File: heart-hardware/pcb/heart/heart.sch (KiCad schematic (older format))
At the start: 64 parts, among them J1 3V0, J2 DIO, J3 CLK, J4 GND, J5 TOUCH_KEY, SW1 SW_SPDT, U1 STM32L031F6Px, U2 TCA6416APWR, U3 LIS3DH, U4 Holtek-Semicon-BS812A-1

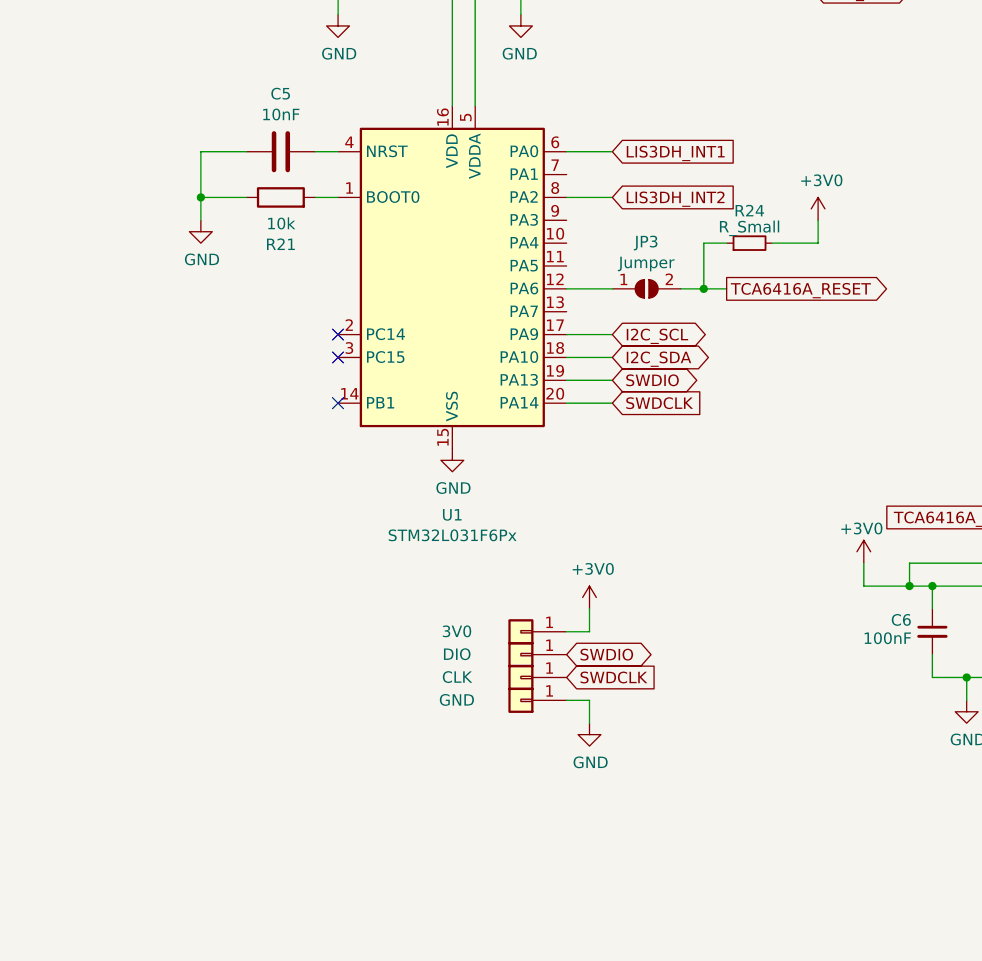
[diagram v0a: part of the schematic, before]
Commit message: Added jumper to choose interuppt lines
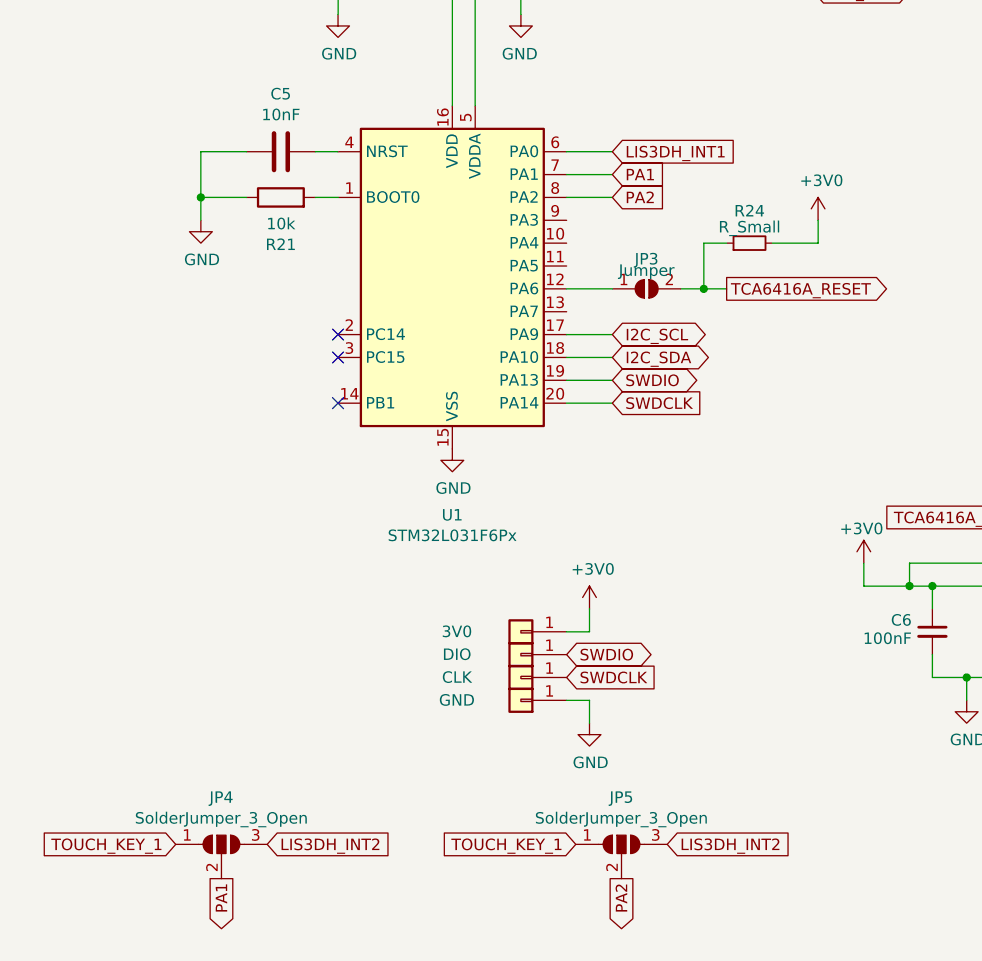
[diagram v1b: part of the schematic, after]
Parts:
- added JP4, JP5: SolderJumper_3_Open, Jumper:SolderJumper-3_P1.3mm_Open_RoundedPad1.0x1.5mm_NumberLabels, symbol Jumper:SolderJumper_3_Open
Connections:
- net LIS3DH_INT2: now also JP4.3 (B), JP5.3 (B); no longer U1.8 (PA2)
- net TOUCH_KEY_1: now also JP4.1 (A), JP5.1 (A)
- net PA1: now reaches U1.7 (PA1)
- net PA1: now also JP4.2 (C)
- new net PA2: JP5.2 (C), U1.8 (PA2)
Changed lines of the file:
@@
 	9100 4300 8700 4300
-Wire Wire Line
-	3100 4300 2900 4300
 Wire Wire Line
 	9500 3900 9500 3800
@@
 	1    0    0    -1
 $EndComp
-Text GLabel 3100 4300 2    50   Input ~ 0
+Text GLabel 1590 7130 2    50   Input ~ 0
 LIS3DH_INT2
 $Comp
@@
 U 1 1 61D85D1A
 P 3250 4700
-F 0 "JP3" H 3250 4905 50  0000 C CNN
-F 1 "Jumper" H 3250 4814 50  0000 C CNN
+F 0 "JP3" H 3250 4830 50  0000 C CNN
+F 1 "Jumper" H 3250 4780 50  0000 C CNN
 F 2 "Jumper:SolderJumper-2_P1.3mm_Open_RoundedPad1.0x1.5mm" H 3250 4700 50  0001 C CNN
 F 3 "~" H 3250 4700 50  0001 C CNN
@@
 Wire Wire Line
 	7600 5700 7910 5700
+Wire Wire Line
+	2900 4300 3100 4300
+$Comp
+L Jumper:SolderJumper_3_Open JP4
+U 1 1 61E88610
+P 1390 7130
+F 0 "JP4" H 1390 7335 50  0000 C CNN
+F 1 "SolderJumper_3_Open" H 1390 7244 50  0000 C CNN
+F 2 "Jumper:SolderJumper-3_P1.3mm_Open_RoundedPad1.0x1.5mm_NumberLabels" H 1390 7130 50  0001 C CNN
+F 3 "~" H 1390 7130 50  0001 C CNN
+	1    1390 7130
+	1    0    0    -1
+$EndComp
+Wire Wire Line
+	2900 4200 3100 4200
+Text GLabel 3100 4200 2    50   Input ~ 0
+PA1
+Text GLabel 3100 4300 2    50   Input ~ 0
+PA2
+$Comp
+L Jumper:SolderJumper_3_Open JP5
+U 1 1 61EAF9B5
+P 3140 7130
+F 0 "JP5" H 3140 7335 50  0000 C CNN
+F 1 "SolderJumper_3_Open" H 3140 7244 50  0000 C CNN
+F 2 "Jumper:SolderJumper-3_P1.3mm_Open_RoundedPad1.0x1.5mm_NumberLabels" H 3140 7130 50  0001 C CNN
+F 3 "~" H 3140 7130 50  0001 C CNN
+	1    3140 7130
+	1    0    0    -1
+$EndComp
+Text GLabel 3340 7130 2    50   Input ~ 0
+LIS3DH_INT2
+Text GLabel 1190 7130 0    50   Input ~ 0
+TOUCH_KEY_1
+Text GLabel 2940 7130 0    50   Input ~ 0
+TOUCH_KEY_1
+Text GLabel 1390 7280 3    50   Output ~ 0
+PA1
+Text GLabel 3140 7280 3    50   Output ~ 0
+PA2
 $EndSCHEMATC

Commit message: Version 1.02
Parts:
- BT1: LCSC (none) -> C238100
- C0: LCSC (none) -> C2918508
- C1: footprint Capacitor_SMD:C_0603_1608Metric -> Capacitor_SMD:C_0402_1005Metric
- C10: LCSC (none) -> C295971
- C11, C2, C4, C6, C9: LCSC (none) -> C60474
- C3, C5, C7: LCSC (none) -> C60133
- C8: LCSC (none) -> C15525
- D0, D1, D10, D11, D12, D13, D14, D15, D2, D3, D4, D5, D6, D7, D8, D9: LCSC (none) -> C2846646
- R0, R1, R10, R11, R12, R13, R14, R15, R2, R3, R4, R5, R6, R7, R8, R9: LCSC (none) -> C258126
- R21, R22, R23, R25, R26: LCSC (none) -> C258091
- R24: value R_Small -> 10k; LCSC (none) -> C258091
- SW1: LCSC (none) -> C221841
- U1: LCSC (none) -> C115208
- U2: LCSC (none) -> C130203
- U3: LCSC (none) -> C15134
- U4: LCSC (none) -> C81747
